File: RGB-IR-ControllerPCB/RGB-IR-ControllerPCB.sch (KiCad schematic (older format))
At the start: 16 parts, among them J1 Conn_01x02_Female, J2 Conn_01x01_Female, J3 Conn_01x01_Female, J4 Conn_01x01_Female, J5 Conn_01x01_Female, Q1 IRF540N, Q2 IRF540N, Q3 IRF540N, U1 TSOP17xx

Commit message: Updated PCB and clear deprecate code
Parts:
- removed J1: Conn_01x02_Female, TerminalBlock:TerminalBlock_bornier-2_P5.08mm, symbol Connector:Conn_01x02_Female
- removed J2, J3, J4, J5: Conn_01x01_Female, Connector_Pin:Pin_D1.4mm_L8.5mm_W2.8mm_FlatFork, symbol Connector:Conn_01x01_Female
- added J1: Screw_Terminal_01x02, TerminalBlock:TerminalBlock_Altech_AK300-2_P5.00mm, symbol Connector:Screw_Terminal_01x02
- added J2: Screw_Terminal_01x04, TerminalBlock:TerminalBlock_Altech_AK300-4_P5.00mm, symbol Connector:Screw_Terminal_01x04
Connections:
- net +12V: now also J1.1 (Pin_1), J2.1 (Pin_1)
- net GND: now also J1.2 (Pin_2)
- net GREEN_PIN: now also A1.12 (D9); no longer A1.13 (D10)
- net RED_PIN: now also A1.13 (D10); no longer A1.12 (D9)
- net at Q2.2 (D): now also J2.3 (Pin_3)
- net at Q1.2 (D): now also J2.2 (Pin_2)
- net at Q3.2 (D): now also J2.4 (Pin_4)
- no-connect marks 21 -> 22
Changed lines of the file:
@@
 $EndComp
 $Comp
-L power:GND #PWR0101
+L power:GND #PWR04
 U 1 1 606A1DF2
 P 1600 7550
-F 0 "#PWR0101" H 1600 7300 50  0001 C CNN
+F 0 "#PWR04" H 1600 7300 50  0001 C CNN
 F 1 "GND" H 1605 7377 50  0000 C CNN
 F 2 "" H 1600 7550 50  0001 C CNN
@@
 	1600 7550 1550 7550
 $Comp
-L power:GND #PWR0102
+L power:GND #PWR01
 U 1 1 606A7797
 P 600 5450
-F 0 "#PWR0102" H 600 5200 50  0001 C CNN
+F 0 "#PWR01" H 600 5200 50  0001 C CNN
 F 1 "GND" H 650 5250 50  0000 R CNN
 F 2 "" H 600 5450 50  0001 C CNN
@@
 $EndComp
 $Comp
-L power:+12V #PWR0103
+L power:+12V #PWR03
 U 1 1 606A8AEB
 P 1450 5550
-F 0 "#PWR0103" H 1450 5400 50  0001 C CNN
+F 0 "#PWR03" H 1450 5400 50  0001 C CNN
 F 1 "+12V" H 1465 5723 50  0000 C CNN
 F 2 "" H 1450 5550 50  0001 C CNN
@@
 $EndComp
 $Comp
-L power:+5V #PWR0104
+L power:+5V #PWR06
 U 1 1 606A9E07
 P 1750 5550
-F 0 "#PWR0104" H 1750 5400 50  0001 C CNN
+F 0 "#PWR06" H 1750 5400 50  0001 C CNN
 F 1 "+5V" H 1765 5723 50  0000 C CNN
 F 2 "" H 1750 5550 50  0001 C CNN
@@
 $EndComp
 $Comp
-L power:+5V #PWR0105
+L power:+5V #PWR02
 U 1 1 606AA3ED
 P 1000 5450
-F 0 "#PWR0105" H 1000 5300 50  0001 C CNN
+F 0 "#PWR02" H 1000 5300 50  0001 C CNN
 F 1 "+5V" H 950 5650 50  0000 L CNN
 F 2 "" H 1000 5450 50  0001 C CNN
@@
 	1    0    0    -1
 $EndComp
+Text GLabel 1050 6950 0    50   Output ~ 0
+RED_PIN
 Text GLabel 1050 6850 0    50   Output ~ 0
-RED_PIN
-Text GLabel 1050 6950 0    50   Output ~ 0
 GREEN_PIN
 Text GLabel 1050 7050 0    50   Output ~ 0
@@
 	2800 6450 2700 6450
 $Comp
-L power:GND #PWR0106
+L power:GND #PWR010
 U 1 1 6078840F
 P 3400 5950
-F 0 "#PWR0106" H 3400 5700 50  0001 C CNN
+F 0 "#PWR010" H 3400 5700 50  0001 C CNN
 F 1 "GND" V 3405 5822 50  0000 R CNN
 F 2 "" H 3400 5950 50  0001 C CNN
@@
 $EndComp
 $Comp
-L power:GND #PWR0107
+L power:GND #PWR09
 U 1 1 6078955C
 P 2800 6450
-F 0 "#PWR0107" H 2800 6200 50  0001 C CNN
+F 0 "#PWR09" H 2800 6200 50  0001 C CNN
 F 1 "GND" V 2805 6322 50  0000 R CNN
 F 2 "" H 2800 6450 50  0001 C CNN
@@
 	4000 5550 4000 5450
 $Comp
-L power:GND #PWR0108
+L power:GND #PWR011
 U 1 1 60789AFF
 P 4000 5450
-F 0 "#PWR0108" H 4000 5200 50  0001 C CNN
+F 0 "#PWR011" H 4000 5200 50  0001 C CNN
 F 1 "GND" V 4005 5322 50  0000 R CNN
 F 2 "" H 4000 5450 50  0001 C CNN
@@
 $EndComp
 $Comp
-L power:+12V #PWR0109
+L power:+12V #PWR08
 U 1 1 6080C130
 P 2700 5450
-F 0 "#PWR0109" H 2700 5300 50  0001 C CNN
+F 0 "#PWR08" H 2700 5300 50  0001 C CNN
 F 1 "+12V" H 2750 5650 50  0000 C CNN
 F 2 "" H 2700 5450 50  0001 C CNN
@@
 $EndComp
 $Comp
-L Connector:Conn_01x02_Female J1
-U 1 1 60874EB8
-P 1750 4800
-F 0 "J1" V 1900 4800 50  0000 R CNN
-F 1 "Conn_01x02_Female" V 1800 5100 50  0000 R CNN
-F 2 "TerminalBlock:TerminalBlock_bornier-2_P5.08mm" H 1750 4800 50  0001 C CNN
-F 3 "~" H 1750 4800 50  0001 C CNN
-	1    1750 4800
-	0    -1   -1   0
-$EndComp
-$Comp
-L power:+12V #PWR0110
+L power:+12V #PWR05
 U 1 1 6087ADC9
 P 1750 5000
-F 0 "#PWR0110" H 1750 4850 50  0001 C CNN
+F 0 "#PWR05" H 1750 4850 50  0001 C CNN
 F 1 "+12V" V 1650 5000 50  0000 L CNN
 F 2 "" H 1750 5000 50  0001 C CNN
@@
 $EndComp
 $Comp
-L power:GND #PWR0111
+L power:GND #PWR07
 U 1 1 6087B56C
 P 1850 5000
-F 0 "#PWR0111" H 1850 4750 50  0001 C CNN
+F 0 "#PWR07" H 1850 4750 50  0001 C CNN
 F 1 "GND" V 1750 5000 50  0000 R CNN
 F 2 "" H 1850 5000 50  0001 C CNN
@@
 $EndComp
 $Comp
-L Connector:Conn_01x01_Female J2
-U 1 1 608A8D29
-P 2700 5250
-F 0 "J2" V 2900 5300 50  0000 R CNN
-F 1 "Conn_01x01_Female" V 2800 5600 50  0000 R CNN
-F 2 "Connector_Pin:Pin_D1.4mm_L8.5mm_W2.8mm_FlatFork" H 2700 5250 50  0001 C CNN
-F 3 "~" H 2700 5250 50  0001 C CNN
-	1    2700 5250
-	0    -1   -1   0
-$EndComp
-$Comp
-L Connector:Conn_01x01_Female J3
-U 1 1 608AA3D2
+L Connector:Screw_Terminal_01x04 J2
+U 1 1 606ECFF6
 P 2800 5250
-F 0 "J3" V 3000 5300 50  0000 R CNN
-F 1 "Conn_01x01_Female" V 2900 5600 50  0000 R CNN
-F 2 "Connector_Pin:Pin_D1.4mm_L8.5mm_W2.8mm_FlatFork" H 2800 5250 50  0001 C CNN
+F 0 "J2" V 2764 4962 50  0000 R CNN
+F 1 "Screw_Terminal_01x04" V 2673 4962 50  0000 R CNN
+F 2 "TerminalBlock:TerminalBlock_Altech_AK300-4_P5.00mm" H 2800 5250 50  0001 C CNN
 F 3 "~" H 2800 5250 50  0001 C CNN
 	1    2800 5250
@@
 $EndComp
 $Comp
-L Connector:Conn_01x01_Female J4
-U 1 1 608AA967
-P 2900 5250
-F 0 "J4" V 3100 5300 50  0000 R CNN
-F 1 "Conn_01x01_Female" V 3000 5600 50  0000 R CNN
-F 2 "Connector_Pin:Pin_D1.4mm_L8.5mm_W2.8mm_FlatFork" H 2900 5250 50  0001 C CNN
-F 3 "~" H 2900 5250 50  0001 C CNN
-	1    2900 5250
-	0    -1   -1   0
-$EndComp
-$Comp
-L Connector:Conn_01x01_Female J5
-U 1 1 608AAF24
-P 3000 5250
-F 0 "J5" V 3200 5300 50  0000 R CNN
-F 1 "Conn_01x01_Female" V 3100 5600 50  0000 R CNN
-F 2 "Connector_Pin:Pin_D1.4mm_L8.5mm_W2.8mm_FlatFork" H 3000 5250 50  0001 C CNN
-F 3 "~" H 3000 5250 50  0001 C CNN
-	1    3000 5250
-	0    -1   -1   0
-$EndComp
+L Connector:Screw_Terminal_01x02 J1
+U 1 1 606EE485
+P 1750 4800
+F 0 "J1" V 1714 4612 50  0000 R CNN
+F 1 "Screw_Terminal_01x02" V 1623 4612 50  0000 R CNN
+F 2 "TerminalBlock:TerminalBlock_Altech_AK300-2_P5.00mm" H 1750 4800 50  0001 C CNN
+F 3 "~" H 1750 4800 50  0001 C CNN
+	1    1750 4800
+	0    -1   -1   0
+$EndComp
+NoConn ~ 1650 5550
 $EndSCHEMATC

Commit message: Refactored PCB
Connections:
- net BLUE_PIN: now also A1.12 (D9); no longer A1.14 (D11)
- net GREEN_PIN: now also A1.14 (D11); no longer A1.12 (D9)
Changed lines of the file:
@@
 Text GLabel 1050 6950 0    50   Output ~ 0
 RED_PIN
+Text GLabel 1050 7050 0    50   Output ~ 0
+GREEN_PIN
 Text GLabel 1050 6850 0    50   Output ~ 0
-GREEN_PIN
-Text GLabel 1050 7050 0    50   Output ~ 0
 BLUE_PIN
 Text GLabel 2500 7250 3    50   Input ~ 0

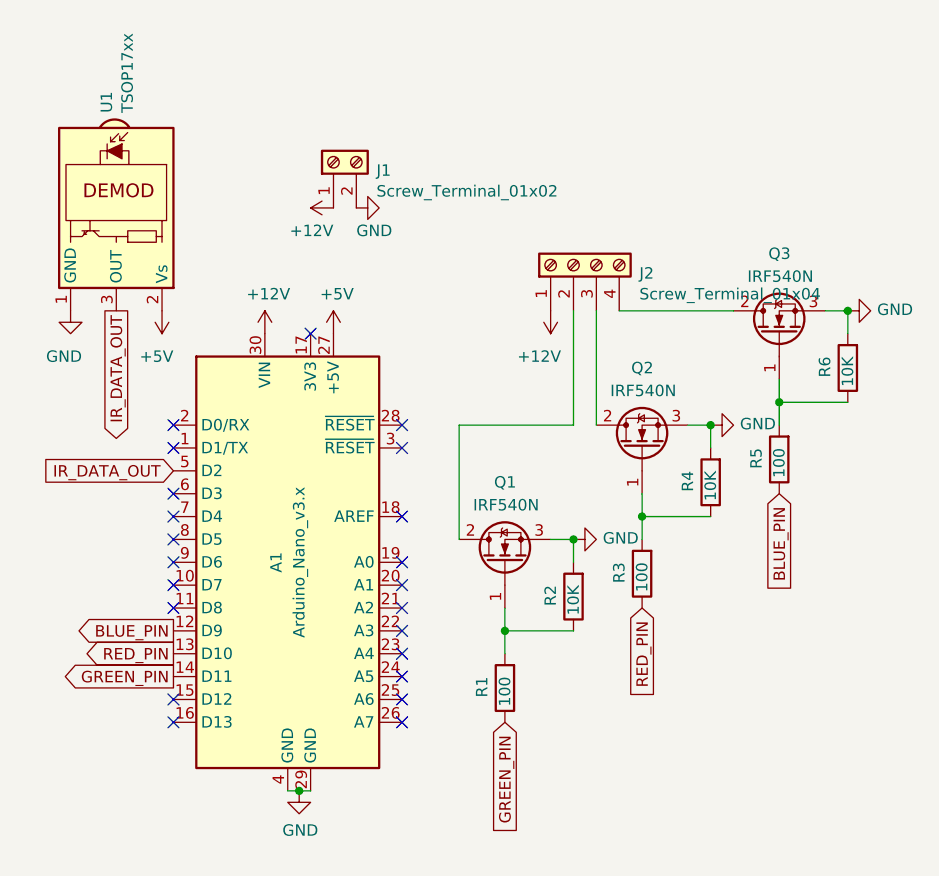
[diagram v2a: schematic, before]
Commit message: updated pcb smd resistors to tht
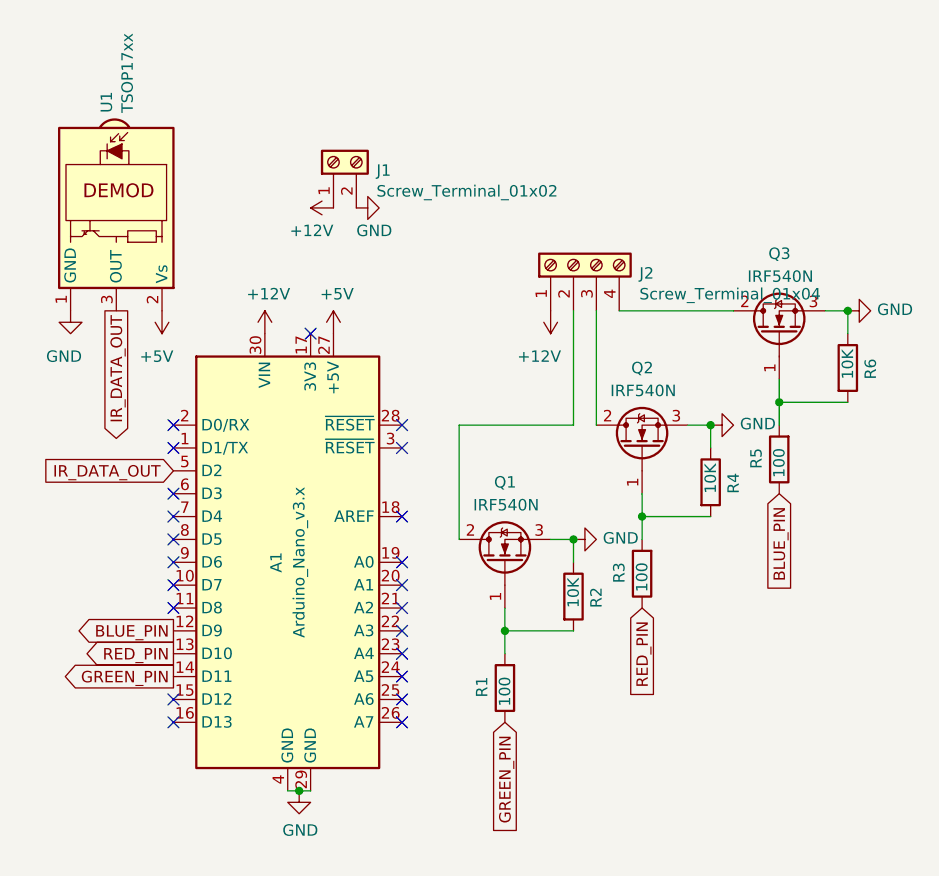
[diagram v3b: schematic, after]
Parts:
- R1, R2, R3, R4, R5, R6: footprint Resistor_SMD:R_0805_2012Metric -> Resistor_THT:R_Axial_DIN0207_L6.3mm_D2.5mm_P10.16mm_Horizontal
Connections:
- net GND: now also R2.1, R4.1, R6.1; no longer R2.2, R4.2, R6.2
- net at Q2.1 (G), R3.2: now also R4.2; no longer R4.1
- net at Q1.1 (G), R1.2: now also R2.2; no longer R2.1
- net at Q3.1 (G), R5.2: now also R6.2; no longer R6.1
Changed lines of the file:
@@
 F 0 "R6" V 4100 5650 50  0000 L CNN
 F 1 "10K" V 4000 5650 50  0000 L CNN
-F 2 "Resistor_SMD:R_0805_2012Metric" V 3930 5700 50  0001 C CNN
+F 2 "Resistor_THT:R_Axial_DIN0207_L6.3mm_D2.5mm_P10.16mm_Horizontal" V 3930 5700 50  0001 C CNN
 F 3 "~" H 4000 5700 50  0001 C CNN
 	1    4000 5700
-	-1   0    0    1
+	1    0    0    -1
 $EndComp
 $Comp
@@
 F 0 "R5" V 3800 6050 50  0000 L CNN
 F 1 "100" V 3700 6050 50  0000 L CNN
-F 2 "Resistor_SMD:R_0805_2012Metric" V 3630 6100 50  0001 C CNN
+F 2 "Resistor_THT:R_Axial_DIN0207_L6.3mm_D2.5mm_P10.16mm_Horizontal" V 3630 6100 50  0001 C CNN
 F 3 "~" H 3700 6100 50  0001 C CNN
 	1    3700 6100
@@
 F 0 "R2" V 2900 6650 50  0000 L CNN
 F 1 "10K" V 2800 6650 50  0000 L CNN
-F 2 "Resistor_SMD:R_0805_2012Metric" V 2730 6700 50  0001 C CNN
+F 2 "Resistor_THT:R_Axial_DIN0207_L6.3mm_D2.5mm_P10.16mm_Horizontal" V 2730 6700 50  0001 C CNN
 F 3 "~" H 2800 6700 50  0001 C CNN
 	1    2800 6700
-	-1   0    0    1
+	1    0    0    -1
 $EndComp
 $Comp
@@
 F 0 "R1" V 2600 7050 50  0000 L CNN
 F 1 "100" V 2500 7050 50  0000 L CNN
-F 2 "Resistor_SMD:R_0805_2012Metric" V 2430 7100 50  0001 C CNN
+F 2 "Resistor_THT:R_Axial_DIN0207_L6.3mm_D2.5mm_P10.16mm_Horizontal" V 2430 7100 50  0001 C CNN
 F 3 "~" H 2500 7100 50  0001 C CNN
 	1    2500 7100
@@
 F 0 "R4" V 3500 6150 50  0000 L CNN
 F 1 "10K" V 3400 6150 50  0000 L CNN
-F 2 "Resistor_SMD:R_0805_2012Metric" V 3330 6200 50  0001 C CNN
+F 2 "Resistor_THT:R_Axial_DIN0207_L6.3mm_D2.5mm_P10.16mm_Horizontal" V 3330 6200 50  0001 C CNN
 F 3 "~" H 3400 6200 50  0001 C CNN
 	1    3400 6200
-	-1   0    0    1
+	1    0    0    -1
 $EndComp
 Text GLabel 3100 6750 3    50   Input ~ 0
@@
 F 0 "R3" V 3200 6550 50  0000 L CNN
 F 1 "100" V 3100 6550 50  0000 L CNN
-F 2 "Resistor_SMD:R_0805_2012Metric" V 3030 6600 50  0001 C CNN
+F 2 "Resistor_THT:R_Axial_DIN0207_L6.3mm_D2.5mm_P10.16mm_Horizontal" V 3030 6600 50  0001 C CNN
 F 3 "~" H 3100 6600 50  0001 C CNN
 	1    3100 6600

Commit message: Added 5V Voltage Regulator
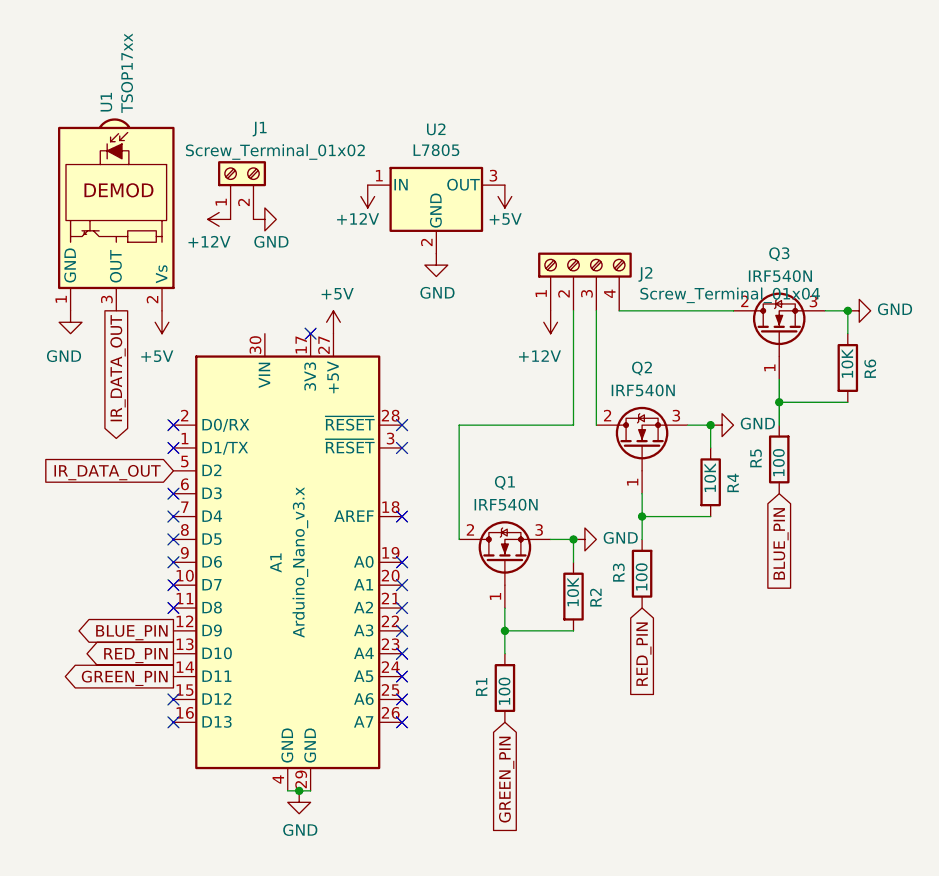
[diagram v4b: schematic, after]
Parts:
- added U2: L7805, Package_TO_SOT_THT:TO-220-3_Vertical, symbol Regulator_Linear:L7805
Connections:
- net +12V: now also U2.1 (IN); no longer A1.30 (VIN)
- net +5V: now also U2.3 (OUT)
- net GND: now also U2.2 (GND)
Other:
- moved on the sheet: J1
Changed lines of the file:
@@
-$EndComp
-$Comp
-L power:+12V #PWR03
-U 1 1 606A8AEB
-P 1450 5550
-F 0 "#PWR03" H 1450 5400 50  0001 C CNN
-F 1 "+12V" H 1465 5723 50  0000 C CNN
-F 2 "" H 1450 5550 50  0001 C CNN
-F 3 "" H 1450 5550 50  0001 C CNN
-	1    1450 5550
-	1    0    0    -1
 $EndComp
 $Comp
@@
 L power:+12V #PWR05
 U 1 1 6087ADC9
-P 1750 5000
-F 0 "#PWR05" H 1750 4850 50  0001 C CNN
-F 1 "+12V" V 1650 5000 50  0000 L CNN
-F 2 "" H 1750 5000 50  0001 C CNN
-F 3 "" H 1750 5000 50  0001 C CNN
-	1    1750 5000
+P 1300 5050
+F 0 "#PWR05" H 1300 4900 50  0001 C CNN
+F 1 "+12V" V 1200 5050 50  0000 L CNN
+F 2 "" H 1300 5050 50  0001 C CNN
+F 3 "" H 1300 5050 50  0001 C CNN
+	1    1300 5050
 	0    -1   -1   0
 $EndComp
@@
 L power:GND #PWR07
 U 1 1 6087B56C
-P 1850 5000
-F 0 "#PWR07" H 1850 4750 50  0001 C CNN
-F 1 "GND" V 1750 5000 50  0000 R CNN
-F 2 "" H 1850 5000 50  0001 C CNN
-F 3 "" H 1850 5000 50  0001 C CNN
-	1    1850 5000
+P 1400 5050
+F 0 "#PWR07" H 1400 4800 50  0001 C CNN
+F 1 "GND" V 1300 5050 50  0000 R CNN
+F 2 "" H 1400 5050 50  0001 C CNN
+F 3 "" H 1400 5050 50  0001 C CNN
+	1    1400 5050
 	0    -1   -1   0
 $EndComp
@@
 L Connector:Screw_Terminal_01x02 J1
 U 1 1 606EE485
-P 1750 4800
-F 0 "J1" V 1714 4612 50  0000 R CNN
-F 1 "Screw_Terminal_01x02" V 1623 4612 50  0000 R CNN
-F 2 "TerminalBlock:TerminalBlock_Altech_AK300-2_P5.00mm" H 1750 4800 50  0001 C CNN
-F 3 "~" H 1750 4800 50  0001 C CNN
-	1    1750 4800
+P 1300 4850
+F 0 "J1" V 1500 4750 50  0000 R CNN
+F 1 "Screw_Terminal_01x02" V 1400 5050 50  0000 R CNN
+F 2 "TerminalBlock:TerminalBlock_Altech_AK300-2_P5.00mm" H 1300 4850 50  0001 C CNN
+F 3 "~" H 1300 4850 50  0001 C CNN
+	1    1300 4850
 	0    -1   -1   0
 $EndComp
 NoConn ~ 1650 5550
+$Comp
+L power:+12V #PWR0101
+U 1 1 607DDD4F
+P 1900 4900
+F 0 "#PWR0101" H 1900 4750 50  0001 C CNN
+F 1 "+12V" H 1850 5050 50  0000 L CNN
+F 2 "" H 1900 4900 50  0001 C CNN
+F 3 "" H 1900 4900 50  0001 C CNN
+	1    1900 4900
+	-1   0    0    1
+$EndComp
+$Comp
+L power:+5V #PWR0102
+U 1 1 607DEAAA
+P 2500 4900
+F 0 "#PWR0102" H 2500 4750 50  0001 C CNN
+F 1 "+5V" H 2500 5050 50  0000 C CNN
+F 2 "" H 2500 4900 50  0001 C CNN
+F 3 "" H 2500 4900 50  0001 C CNN
+	1    2500 4900
+	-1   0    0    1
+$EndComp
+$Comp
+L power:GND #PWR0103
+U 1 1 607E4EDD
+P 2200 5200
+F 0 "#PWR0103" H 2200 4950 50  0001 C CNN
+F 1 "GND" H 2205 5027 50  0000 C CNN
+F 2 "" H 2200 5200 50  0001 C CNN
+F 3 "" H 2200 5200 50  0001 C CNN
+	1    2200 5200
+	1    0    0    -1
+$EndComp
+$Comp
+L Regulator_Linear:L7805 U2
+U 1 1 607D85A8
+P 2200 4900
+F 0 "U2" H 2200 5142 50  0000 C CNN
+F 1 "L7805" H 2200 5051 50  0000 C CNN
+F 2 "Package_TO_SOT_THT:TO-220-3_Vertical" H 2225 4750 50  0001 L CIN
+F 3 "http://www.st.com/content/ccc/resource/technical/document/datasheet/41/4f/b3/b0/12/d4/47/88/CD00000444.pdf/files/CD00000444.pdf/jcr:content/translations/en.CD00000444.pdf" H 2200 4850 50  0001 C CNN
+	1    2200 4900
+	1    0    0    -1
+$EndComp
 $EndSCHEMATC
